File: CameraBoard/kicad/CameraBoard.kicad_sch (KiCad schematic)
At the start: 0 parts

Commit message: changes to lv3.2 camera board
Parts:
- added C1: 100nf, Capacitor_SMD:C_0603_1608Metric, symbol Device:C_Small
- added C14: 10n, CameraBoard:.0603-A-NOSILK, symbol Device:C
- added C15, C16, C17, C18: 10u, CameraBoard:.0805-B-NOSILK, symbol Device:C
- added C19, C20, C21: 47u, CameraBoard:1206-A, symbol Device:C
- added C2: 2.2u, Capacitor_SMD:C_1206_3216Metric, symbol Device:C_Small
- added C3: 1u, Capacitor_SMD:C_0603_1608Metric, symbol Device:C_Small
- added C4: 1uf 0805, Capacitor_SMD:C_0805_2012Metric, symbol Device:C_Small
- added C9: 10uf 1206, Capacitor_SMD:C_1206_3216Metric, symbol Device:C_Small
- added D1, D3: LED, CameraBoard:CHIPLED_0603_259, symbol Device:LED_Small_Filled
- added D2: LED_Small_Filled, CameraBoard:CHIPLED_0603_259, symbol Device:LED_Small_Filled
- added D4: SS24, Diode_SMD:D_SMA, symbol Diode:SS24
- added D6: D_MBRS340T3G, Diode_SMD:D_SMC, symbol Diode:MBRS340
- added IC1: MP2659GQ-0000-Z, MP2659GQ0000Z, symbol MP2659GQ-0000-Z:MP2659GQ-0000-Z
- added JP1, JP10, JP12, JP13, JP2, JP3, JP4, JP5, JP6, JP7: PINHD-1X3, Connector_PinHeader_2.54mm:PinHeader_1x03_P2.54mm_Vertical_SMD_Pin1Left, symbol Connector_Generic:Conn_01x03
- added JP14: (no value), Connector_PinHeader_2.54mm:PinHeader_1x02_P2.54mm_Vertical_SMD_Pin1Left, symbol Connector_Generic:Conn_01x02
- added JP18, JP19: PINHD-1X6, Connector_PinHeader_2.54mm:PinHeader_1x06_P2.54mm_Vertical, symbol Connector_Generic:Conn_01x06
- added L1: 10uh or 3.3uh, Inductor_SMD:L_0603_1608Metric, symbol Device:L_Small
- added L3: 784770220, CameraBoard:784770220, symbol CameraBoard-eagle-import:784770220
- added Q2, Q4: SI7465DP-T1-E3, CameraBoard:SI7465DP-T1-E3CT-ND, symbol CameraBoard-eagle-import:SI7465DP-T1-E3
- added R1: 2.26k, Resistor_SMD:R_0603_1608Metric, symbol Device:R_Small_US
- added R16, R17: 750, Resistor_SMD:R_0603_1608Metric, symbol Device:R_Small_US
- added R19, R33: 150k, Resistor_SMD:R_0603_1608Metric, symbol Device:R_Small_US
- added R2: 6.95k, Resistor_SMD:R_0603_1608Metric, symbol Device:R_Small_US
- added R3: 38.4k, Resistor_SMD:R_0603_1608Metric, symbol Device:R_Small_US
- added R31, R32: 1k, Resistor_SMD:R_0603_1608Metric, symbol Device:R_Small_US
- added R4, R5: 10k, Resistor_SMD:R_0603_1608Metric, symbol Device:R_Small_US
- added R6: 133k, Resistor_SMD:R_0603_1608Metric, symbol Device:R_Small_US
- added R7: 33k, Resistor_SMD:R_0603_1608Metric, symbol Device:R_Small_US
- added TH1: 10k, Resistor_SMD:R_0603_1608Metric, symbol Device:Thermistor_NTC
- added TP1: (no value), TestPoint:TestPoint_Plated_Hole_D2.0mm, symbol oresat-misc:Test-Point-0.75mm-th
- added TP11, TP12, TP2: TEST-POINT, TestPoint:TestPoint_Plated_Hole_D2.0mm, symbol oresat-misc:Test-Point-0.75mm-th
- added U3: LM2678SD-12/NOPB, CameraBoard:LM2678SD-12_NOPB, symbol CameraBoard-eagle-import:LM2678SD-12/NOPB
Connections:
- new net: C2.2, D4.1 (K), IC1.19 (PMID_S), IC1.2 (PMID)
- new net: Q4.G, R31.1, R33.2
- new net: IC1.13 (NTC), R1.2, R2.1, TH1.1
- new net: C14.2, U3.4 (CB)
- new net: TP1.1, U3.8 (ON)
- new net: D1.1 (K), JP10.3 (Pin_3)
- new net: D1.2 (A), R16.2
- new net: C9.1, JP18.4 (Pin_4), JP18.5 (Pin_5), JP18.6 (Pin_6)
- new net: C1.1, IC1.4 (BST)
- new net: C1.2, IC1.3 (SW), L1.1
- new net: IC1.15 (ISET), R3.1
- new net: IC1.17 (ILIM), R7.2
- new net: IC1.18 (VDPM), R5.2, R6.1
- new net: D2.1 (K), IC1.9 (~{ACOK})
- new net: D3.2 (A), R17.2
- new net: D2.2 (A), R4.2
- new net: JP14.2 (Pin_2), Q2.G, R19.2
- new net +12V: C19.1, C20.1, C21.1, JP1.1 (Pin_1), JP10.1 (Pin_1), JP12.1 (Pin_1), JP13.1 (Pin_1), JP2.1 (Pin_1), JP3.1 (Pin_1), JP4.1 (Pin_1), JP5.1 (Pin_1), JP6.1 (Pin_1), JP7.1 (Pin_1), L3.P2 (P$2), TP2.1, U3.7 (FB)
- new net +16V: Q2.D1 (D), Q2.D2 (D), Q2.D3 (D), Q2.D4 (D), Q2.DPAD (D), Q4.D1 (D), Q4.D2 (D), Q4.D3 (D), Q4.D4 (D), Q4.DPAD (D)
- new net ARM-IN: JP19.6 (Pin_6), R31.2
- new net ARM-OUT: JP19.5 (Pin_5), R32.1
- new net BATT+: C15.1, C16.1, C17.1, C18.1, IC1.14 (BATT), JP18.1 (Pin_1), JP18.2 (Pin_2), JP18.3 (Pin_3), L1.2, Q2.S1 (S), Q2.S2 (S), Q2.S3 (S), Q4.S1 (S), Q4.S2 (S), Q4.S3 (S), R32.2, U3.2 (IN), U3.3 (IN)
- new net CAM_DOWN: JP12.3 (Pin_3), R16.1, TP11.1
- new net CAM_UP: JP13.3 (Pin_3), R17.1, TP12.1
- new net CHUTE: JP19.2 (Pin_2)
- new net DROGUE: JP19.3 (Pin_3)
- new net GND: C15.2, C16.2, C17.2, C18.2, C19.2, C2.1, C20.2, C21.2, C3.2, C4.2, C9.2, D3.1 (K), D6.2 (A), IC1.12 (AGND), IC1.5 (PGND_1), IC1.6 (PGND_2), IC1.7 (PGND_3), JP1.2 (Pin_2), JP10.2 (Pin_2), JP12.2 (Pin_2), JP13.2 (Pin_2), JP14.1 (Pin_1), JP2.2 (Pin_2), JP3.2 (Pin_2), JP4.2 (Pin_2), JP5.2 (Pin_2), JP6.2 (Pin_2), JP7.2 (Pin_2), R19.1, R2.2, R3.2, R33.1, R5.1, R7.1, TH1.2, U3.9 (GND), U3.DAP (GND)
- new net SOUT: C14.1, D6.1 (K), L3.P1 (P$1), U3.12 (SOUT), U3.13 (SOUT), U3.14 (SOUT)
- new net T_GND: JP19.1 (Pin_1)
- new net VCC: C3.1, IC1.16 (VCC), IC1.8 (~{STAT}), R1.1
- new net VUMB: C4.1, D4.2 (A), IC1.1 (IN), JP19.4 (Pin_4), R4.1, R6.2
- no-connect marks 0 -> 10
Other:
- removed sheet CameraBoard_1
- removed sheet CameraBoard_2
- note added: "12V @ 5A Max"
- note added: "16.8V to 12V SPS"
- note added: "4S Battery Pack"
- note added: "4S LiPo Charger"
- note added: "ARM + TELEMETRUM + VUMB"
- note added: "ARM+ ARM- VUMB DROGUE CHUTE TGND"
- note added: "All resistors are 1% 0603 packages unless otherwise specified All capacitors are 10% 0603 packages unless otherwise specified"
- note added: "Camera Operation"
- note added: "Cameras"
- note added: "Comp selection: -Datasheet called for polarized -The diode has 4A rating"
- note added: "Keep feedback wire away from inductor flux on board"
- note added: "Rocket Ready"
- note added: "TO ATV TX: 7-36V"
- note added: "Wired into 12V because it was easy; might be better directly to vbatt."
- note added: "cell count setting"
- note added: "charge reg. volt setting"
- company: (none) -> Portland State Aerospace Society
- title: (none) -> LV3 Camera Board

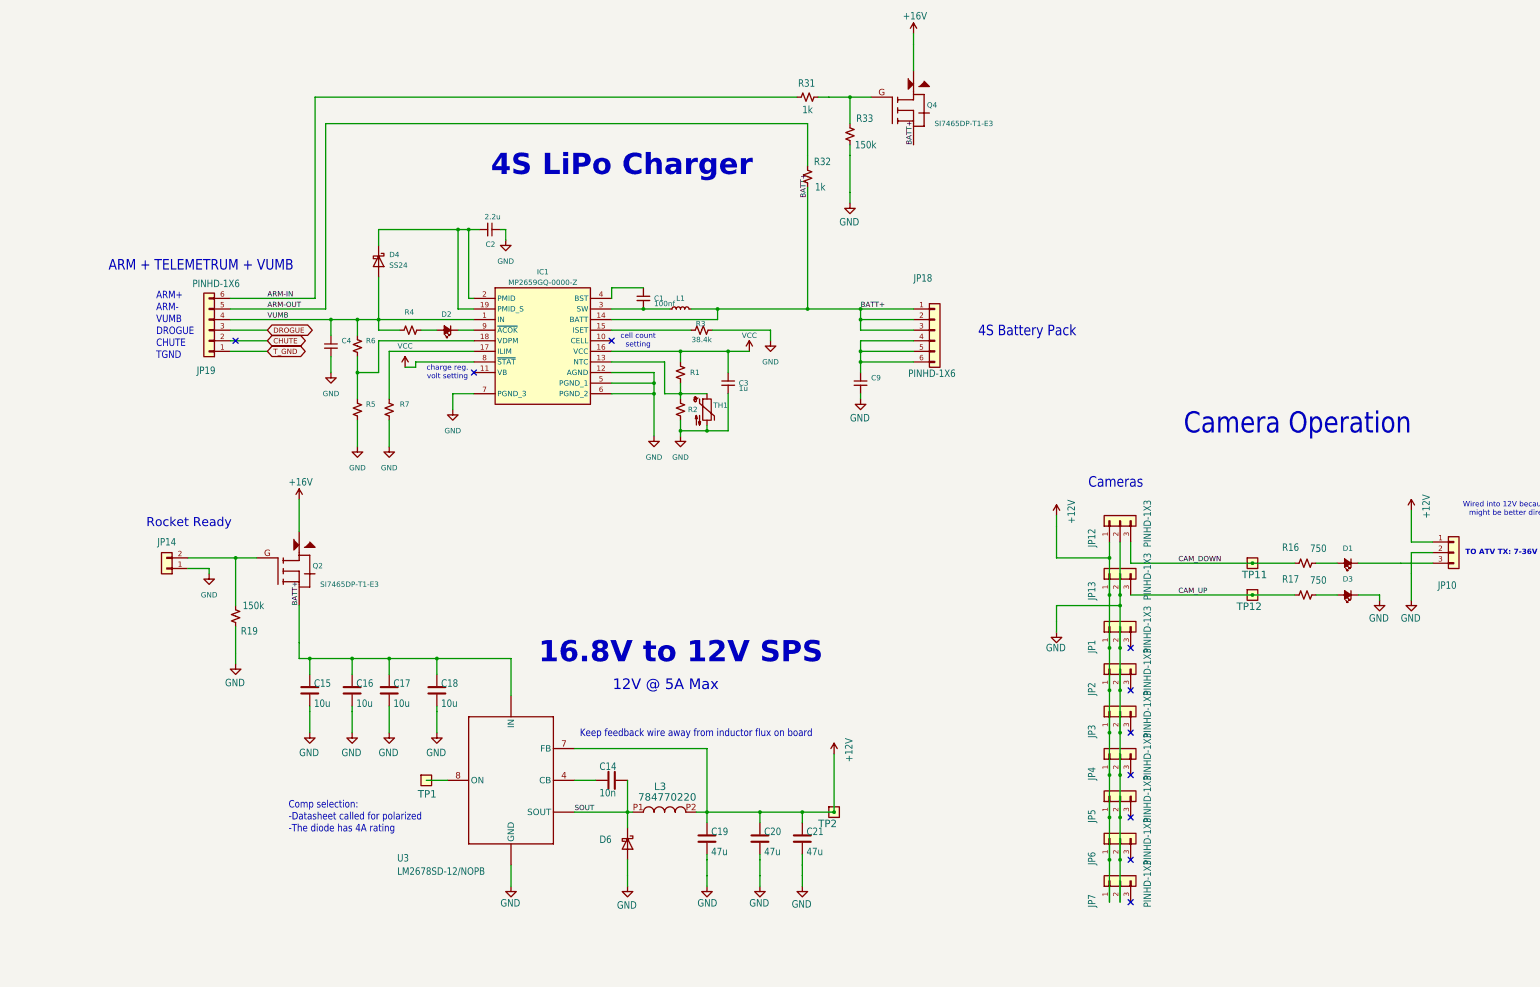
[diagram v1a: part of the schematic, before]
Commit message: Minor updates to schematic
Removed connectors
Changed SPS layout
Added and removed LEDs
Edited labels
Fixed IC application
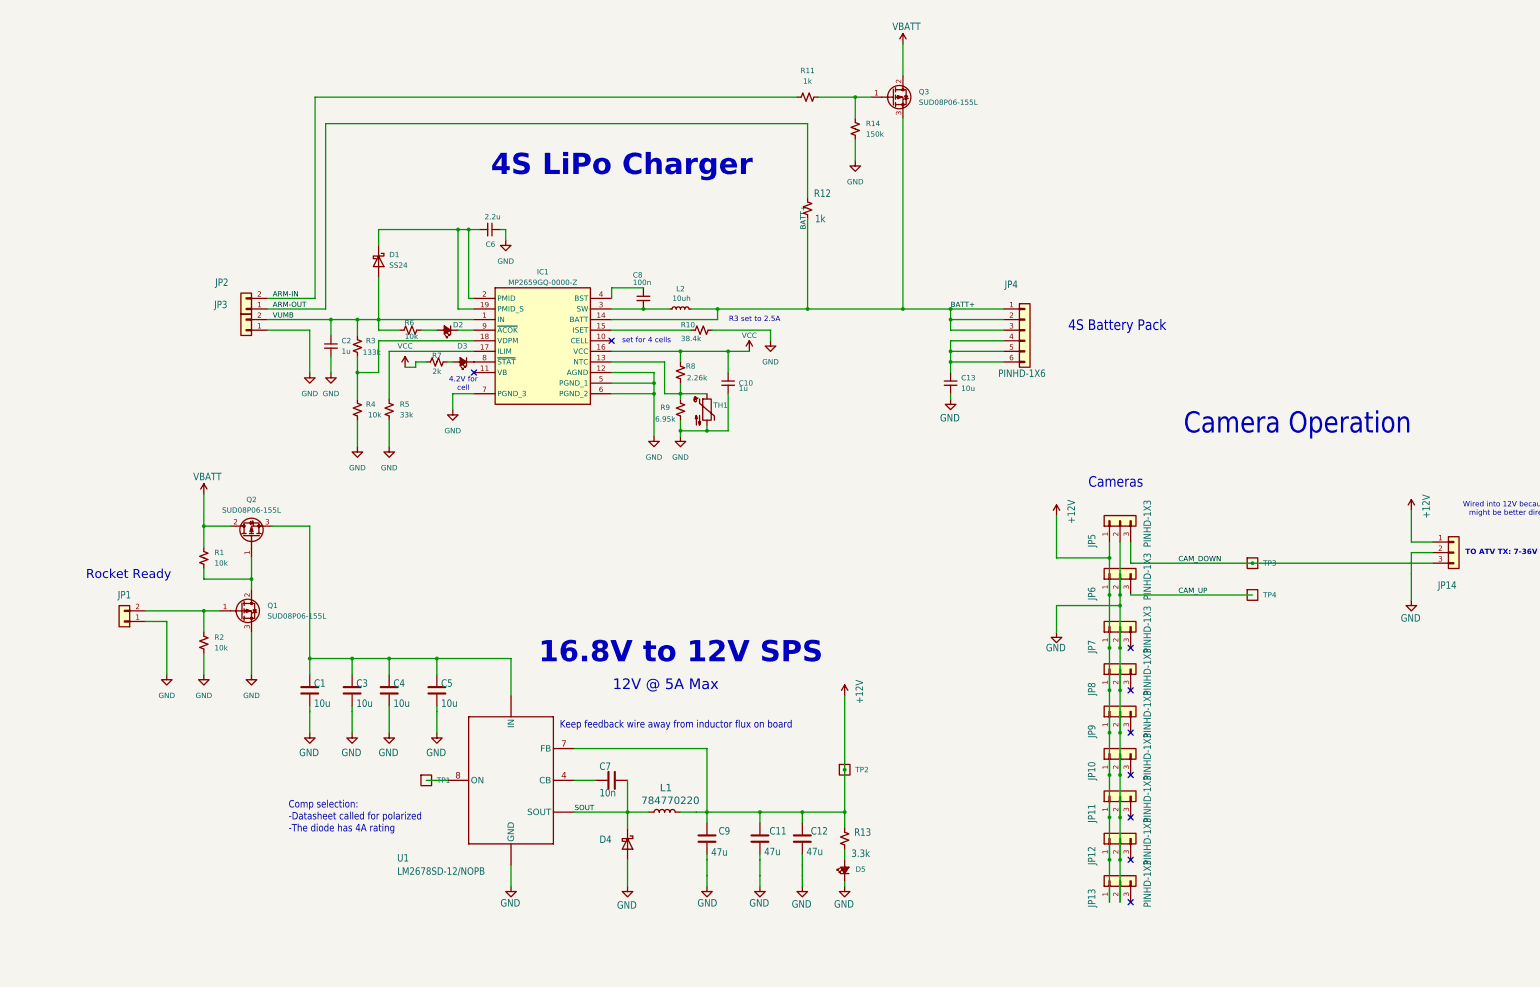
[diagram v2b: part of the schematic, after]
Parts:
- removed D1: LED, CameraBoard:CHIPLED_0603_259, symbol Device:LED_Small_Filled
- removed JP14: (no value), Connector_PinHeader_2.54mm:PinHeader_1x02_P2.54mm_Vertical_SMD_Pin1Left, symbol Connector_Generic:Conn_01x02
- removed JP19: PINHD-1X6, Connector_PinHeader_2.54mm:PinHeader_1x06_P2.54mm_Vertical, symbol Connector_Generic:Conn_01x06
- removed Q2, Q4: SI7465DP-T1-E3, CameraBoard:SI7465DP-T1-E3CT-ND, symbol CameraBoard-eagle-import:SI7465DP-T1-E3
- removed R16, R17: 750, Resistor_SMD:R_0603_1608Metric, symbol Device:R_Small_US
- removed R19, R33: 150k, Resistor_SMD:R_0603_1608Metric, symbol Device:R_Small_US
- removed R31, R32: 1k, Resistor_SMD:R_0603_1608Metric, symbol Device:R_Small_US
- removed TP1: (no value), TestPoint:TestPoint_Plated_Hole_D2.0mm, symbol oresat-misc:Test-Point-0.75mm-th
- removed TP11, TP12, TP2: TEST-POINT, TestPoint:TestPoint_Plated_Hole_D2.0mm, symbol oresat-misc:Test-Point-0.75mm-th
- added D5: LED_Small_Filled, CameraBoard:CHIPLED_0603_259, symbol Device:LED_Small_Filled
- added JP1, JP2, JP3: (no value), Connector_PinHeader_2.54mm:PinHeader_1x02_P2.54mm_Vertical_SMD_Pin1Left, symbol Connector_Generic:Conn_01x02
- added Q1, Q2, Q3: SUD08P06-155L, Package_TO_SOT_SMD:TO-252-2, symbol Transistor_FET:SUD08P06-155L
- added R1, R2: 10k, Resistor_SMD:R_0603_1608Metric, symbol Device:R_Small_US
- added R11, R12: 1k, Resistor_SMD:R_0603_1608Metric, symbol Device:R_Small_US
- added R13: 3.3k, Resistor_SMD:R_0603_1608Metric, symbol Device:R_Small_US
- added R14: 150k, Resistor_SMD:R_0603_1608Metric, symbol Device:R_Small_US
- added R7: 2k, Resistor_SMD:R_0603_1608Metric, symbol Device:R_Small_US
- added TP1, TP2, TP3, TP4: Test-Point, CameraBoard:2MM-TEST-POINT, symbol psas-testpoint:Test-Point
- C13: renamed from C9; value 10uf 1206 -> 10u
- C2: renamed from C4; value 1uf 0805 -> 1u
- C8: renamed from C1; value 100nf -> 100n
- D3: value LED -> LED_Small_Filled
- L1: renamed from L3; symbol CameraBoard-eagle-import:784770220 -> Device:L
- L2: renamed from L1; value 10uh or 3.3uh -> 10uh
- renumbered C15 to C1, C3 to C10, C20 to C11, C21 to C12, C16 to C3, C17 to C4, C18 to C5, C2 to C6, C14 to C7, C19 to C9, D4 to D1, D6 to D4, JP4 to JP10, JP5 to JP11, JP6 to JP12, JP7 to JP13, JP10 to JP14, JP18 to JP4, JP12 to JP5, JP13 to JP6, JP1 to JP7, JP2 to JP8, JP3 to JP9, R3 to R10, R6 to R3, R5 to R4, R7 to R5, R4 to R6, R1 to R8, R2 to R9, U3 to U1
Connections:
- net +12V: now also L1.2, R13.2, TP2.1; no longer L1.P2 (P$2)
- net ARM-IN: now also JP2.2 (Pin_2), R11.1
- net ARM-OUT: now also JP2.1 (Pin_1), R12.1
- net BATT+: now also Q3.3 (S), R12.2; no longer C1.1, C3.1, C4.1, C5.1, U1.2 (IN), U1.3 (IN)
- net CAM_DOWN: now also JP14.3 (Pin_3), TP3.1
- net CAM_UP: now also TP4.1
- net GND: now also D5.1 (K), JP1.1 (Pin_1), JP3.1 (Pin_1), Q1.3 (S), R14.2, R2.2; no longer D3.1 (K)
- net SOUT: now also L1.1; no longer L1.P1 (P$1)
- net VCC: now also R7.1; no longer IC1.8 (~{STAT})
- net VUMB: now also JP3.2 (Pin_2)
- net at U1.8 (ON): now also TP1.1
- net at D3.2 (A): now also R7.2
- new net: C1.1, C3.1, C4.1, C5.1, Q2.3 (S), U1.2 (IN), U1.3 (IN)
- new net: Q3.1 (G), R11.2, R14.1
- new net: Q1.2 (D), Q2.1 (G), R1.2
- new net: D5.2 (A), R13.1
- new net: JP1.2 (Pin_2), Q1.1 (G), R2.1
- new net: D3.1 (K), IC1.8 (~{STAT})
- new net VBATT: Q2.2 (D), Q3.2 (D), R1.1
- no-connect marks 10 -> 9
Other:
- note added: "4.2V for cell"
- note added: "R3 set to 2.5A"
- note added: "set for 4 cells"
- note removed: "ARM + TELEMETRUM + VUMB"
- note removed: "ARM+ ARM- VUMB DROGUE CHUTE TGND"
- note removed: "cell count setting"
- note removed: "charge reg. volt setting"
- moved on the sheet: C13, JP4

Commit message: Schematic Clean-up
Straightened up text, symbols, etc.
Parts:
- removed D1: SS24, Diode_SMD:D_SMA, symbol Diode:SS24
- added D6: B240, Diode_SMD:D_SMB, symbol Diode:B240
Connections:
- net VUMB: now also D6.2 (A)
- net at C6.2, IC1.19 (PMID_S), IC1.2 (PMID): now also D6.1 (K)
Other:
- note added: "R10 set to 2.5A"
- note removed: "R3 set to 2.5A"
- moved on the sheet: D3, R7
